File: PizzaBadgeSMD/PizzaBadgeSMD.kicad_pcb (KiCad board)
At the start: 2 copper layers, 52 x 52 mm, 168 parts, among them Q1 NPN, Q2 NPN, Q3 NPN, Q4 NPN, Q5 NPN, Q6 NPN, Q7 NPN, Q8 NPN, SW1 RESET, U1 ESP-12E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

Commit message: fill board
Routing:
- added copper zone on B.Cu, net GND
- added copper zone on F.Cu, net GND

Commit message: update SMD version
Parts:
- added R82: 10K, Resistor_SMD:R_0805_2012Metric, B.Cu at (151.2, 93.6)
- added R83: 10K, Resistor_SMD:R_0805_2012Metric, B.Cu at (125.2, 95.4)
- moved R20 0.60 mm to (155.2, 87.2)
- moved R30 0.54 mm to (155.3, 101.0)
- moved R70 0.50 mm to (122.0, 87.4)
- moved R80 0.41 mm to (131.5, 77.9)
- renumbered GND to J1, 5V to J2
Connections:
- R1 pad 2: Net-(Q1-Pad1) -> Net-(Q1-Pad2)
- R10 pad 1: Net-(Q1-Pad2) -> Net-(Q1-Pad1)
- R11 pad 2: Net-(Q2-Pad1) -> Net-(Q2-Pad2)
- R12 pad 2: Net-(Q2-Pad1) -> Net-(Q2-Pad2)
- R13 pad 2: Net-(Q2-Pad1) -> Net-(Q2-Pad2)
- R14 pad 2: Net-(Q2-Pad1) -> Net-(Q2-Pad2)
- R15 pad 2: Net-(Q2-Pad1) -> Net-(Q2-Pad2)
- R16 pad 2: Net-(Q2-Pad1) -> Net-(Q2-Pad2)
- R17 pad 2: Net-(Q2-Pad1) -> Net-(Q2-Pad2)
- R18 pad 2: Net-(Q2-Pad1) -> Net-(Q2-Pad2)
- R19 pad 2: Net-(Q2-Pad1) -> Net-(Q2-Pad2)
- R2 pad 2: Net-(Q1-Pad1) -> Net-(Q1-Pad2)
- R20 pad 1: Net-(Q2-Pad2) -> Net-(Q2-Pad1)
- R21 pad 2: Net-(Q3-Pad1) -> Net-(Q3-Pad2)
- R22 pad 2: Net-(Q3-Pad1) -> Net-(Q3-Pad2)
- R23 pad 2: Net-(Q3-Pad1) -> Net-(Q3-Pad2)
- R24 pad 2: Net-(Q3-Pad1) -> Net-(Q3-Pad2)
- R25 pad 2: Net-(Q3-Pad1) -> Net-(Q3-Pad2)
- R26 pad 2: Net-(Q3-Pad1) -> Net-(Q3-Pad2)
- R27 pad 2: Net-(Q3-Pad1) -> Net-(Q3-Pad2)
- R28 pad 2: Net-(Q3-Pad1) -> Net-(Q3-Pad2)
- R29 pad 2: Net-(Q3-Pad1) -> Net-(Q3-Pad2)
- R3 pad 2: Net-(Q1-Pad1) -> Net-(Q1-Pad2)
- R30 pad 1: Net-(Q3-Pad2) -> Net-(Q3-Pad1)
- R31 pad 2: Net-(Q4-Pad1) -> Net-(Q4-Pad2)
- R32 pad 2: Net-(Q4-Pad1) -> Net-(Q4-Pad2)
- R33 pad 2: Net-(Q4-Pad1) -> Net-(Q4-Pad2)
- R34 pad 2: Net-(Q4-Pad1) -> Net-(Q4-Pad2)
- R35 pad 2: Net-(Q4-Pad1) -> Net-(Q4-Pad2)
- R36 pad 2: Net-(Q4-Pad1) -> Net-(Q4-Pad2)
- R37 pad 2: Net-(Q4-Pad1) -> Net-(Q4-Pad2)
- R38 pad 2: Net-(Q4-Pad1) -> Net-(Q4-Pad2)
- R39 pad 1: Net-(Q4-Pad2) -> Net-(Q4-Pad1)
- R4 pad 2: Net-(Q1-Pad1) -> Net-(Q1-Pad2)
- R40 pad 2: Net-(Q4-Pad1) -> Net-(Q4-Pad2)
- R41 pad 2: Net-(Q5-Pad1) -> Net-(Q5-Pad2)
- R42 pad 2: Net-(Q5-Pad1) -> Net-(Q5-Pad2)
- R43 pad 2: Net-(Q5-Pad1) -> Net-(Q5-Pad2)
- R44 pad 2: Net-(Q5-Pad1) -> Net-(Q5-Pad2)
- R45 pad 2: Net-(Q5-Pad1) -> Net-(Q5-Pad2)
- R46 pad 2: Net-(Q5-Pad1) -> Net-(Q5-Pad2)
- R47 pad 2: Net-(Q5-Pad1) -> Net-(Q5-Pad2)
- R48 pad 2: Net-(Q5-Pad1) -> Net-(Q5-Pad2)
- R49 pad 2: Net-(Q5-Pad1) -> Net-(Q5-Pad2)
- R5 pad 2: Net-(Q1-Pad1) -> Net-(Q1-Pad2)
- R50 pad 1: Net-(Q5-Pad2) -> Net-(Q5-Pad1)
- R51 pad 2: Net-(Q6-Pad1) -> Net-(Q6-Pad2)
- R52 pad 2: Net-(Q6-Pad1) -> Net-(Q6-Pad2)
- R53 pad 2: Net-(Q6-Pad1) -> Net-(Q6-Pad2)
- R54 pad 2: Net-(Q6-Pad1) -> Net-(Q6-Pad2)
- R55 pad 2: Net-(Q6-Pad1) -> Net-(Q6-Pad2)
- R56 pad 2: Net-(Q6-Pad1) -> Net-(Q6-Pad2)
- R57 pad 2: Net-(Q6-Pad1) -> Net-(Q6-Pad2)
- R58 pad 2: Net-(Q6-Pad1) -> Net-(Q6-Pad2)
- R59 pad 2: Net-(Q6-Pad1) -> Net-(Q6-Pad2)
- R6 pad 2: Net-(Q1-Pad1) -> Net-(Q1-Pad2)
- R60 pad 1: Net-(Q6-Pad2) -> Net-(Q6-Pad1)
- R61 pad 2: Net-(Q7-Pad1) -> Net-(Q7-Pad2)
- R62 pad 2: Net-(Q7-Pad1) -> Net-(Q7-Pad2)
- R63 pad 2: Net-(Q7-Pad1) -> Net-(Q7-Pad2)
- R64 pad 2: Net-(Q7-Pad1) -> Net-(Q7-Pad2)
- R65 pad 2: Net-(Q7-Pad1) -> Net-(Q7-Pad2)
- R66 pad 2: Net-(Q7-Pad1) -> Net-(Q7-Pad2)
- R67 pad 2: Net-(Q7-Pad1) -> Net-(Q7-Pad2)
- R68 pad 2: Net-(Q7-Pad1) -> Net-(Q7-Pad2)
- R69 pad 2: Net-(Q7-Pad1) -> Net-(Q7-Pad2)
- R7 pad 2: Net-(Q1-Pad1) -> Net-(Q1-Pad2)
- R70 pad 1: Net-(Q7-Pad2) -> Net-(Q7-Pad1)
- R71 pad 2: Net-(Q8-Pad1) -> Net-(Q8-Pad2)
- R72 pad 2: Net-(Q8-Pad1) -> Net-(Q8-Pad2)
- R73 pad 2: Net-(Q8-Pad1) -> Net-(Q8-Pad2)
- R74 pad 2: Net-(Q8-Pad1) -> Net-(Q8-Pad2)
- R75 pad 2: Net-(Q8-Pad1) -> Net-(Q8-Pad2)
- R76 pad 2: Net-(Q8-Pad1) -> Net-(Q8-Pad2)
- R77 pad 2: Net-(Q8-Pad1) -> Net-(Q8-Pad2)
- R78 pad 2: Net-(Q8-Pad1) -> Net-(Q8-Pad2)
- R79 pad 2: Net-(Q8-Pad1) -> Net-(Q8-Pad2)
- R8 pad 2: Net-(Q1-Pad1) -> Net-(Q1-Pad2)
- R80 pad 1: Net-(Q8-Pad2) -> Net-(Q8-Pad1)
- R9 pad 2: Net-(Q1-Pad1) -> Net-(Q1-Pad2)
- U1 pad 3: unconnected-(U1-Pad3) -> Net-(U1-Pad3)
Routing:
- net Net-(Q1-Pad2): track 3.88 -> 47.4 mm
- net Net-(Q6-Pad2): track 5.15 -> 47.4 mm
- net Net-(Q5-Pad2): track 4.79 -> 45.9 mm
- net Net-(Q4-Pad2): track 4.68 -> 45.2 mm
- net Net-(Q3-Pad2): track 4.41 -> 43.8 mm
- net Net-(Q7-Pad2): track 4.60 -> 43.2 mm
- net Net-(Q6-Pad1): track 42.6 -> 4.88 mm
- net Net-(Q3-Pad1): track 41.7 -> 4.09 mm
- net Net-(Q1-Pad1): track 41.8 -> 4.15 mm
- net Net-(Q8-Pad2): track 4.19 -> 41.5 mm
- net Net-(Q4-Pad1): track 41.1 -> 4.13 mm
- net Net-(Q2-Pad2): track 4.68 -> 40.2 mm
- net Net-(Q5-Pad1): track 40.5 -> 5.06 mm
- net Net-(Q8-Pad1): track 41.8 -> 8.84 mm
- net Net-(Q7-Pad1): track 40.3 -> 8.84 mm
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
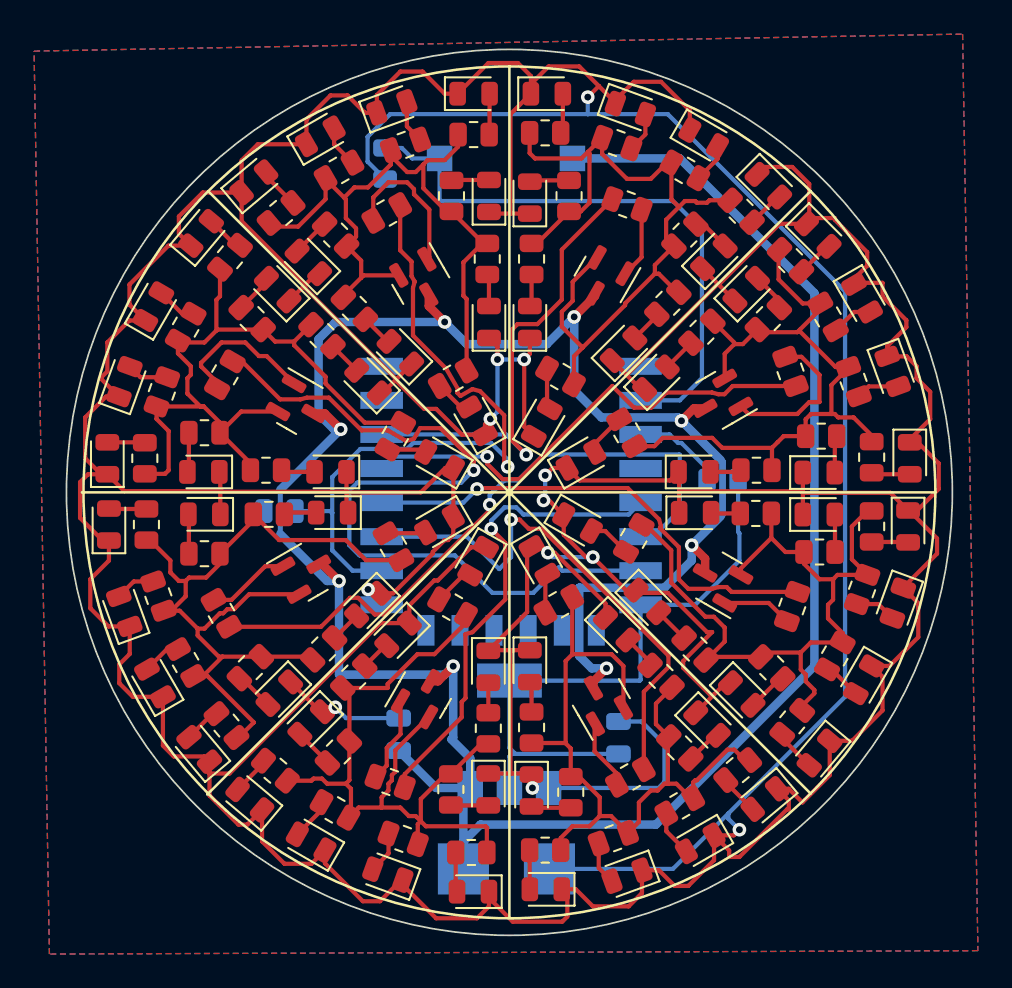
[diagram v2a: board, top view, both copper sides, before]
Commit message: add coin battery
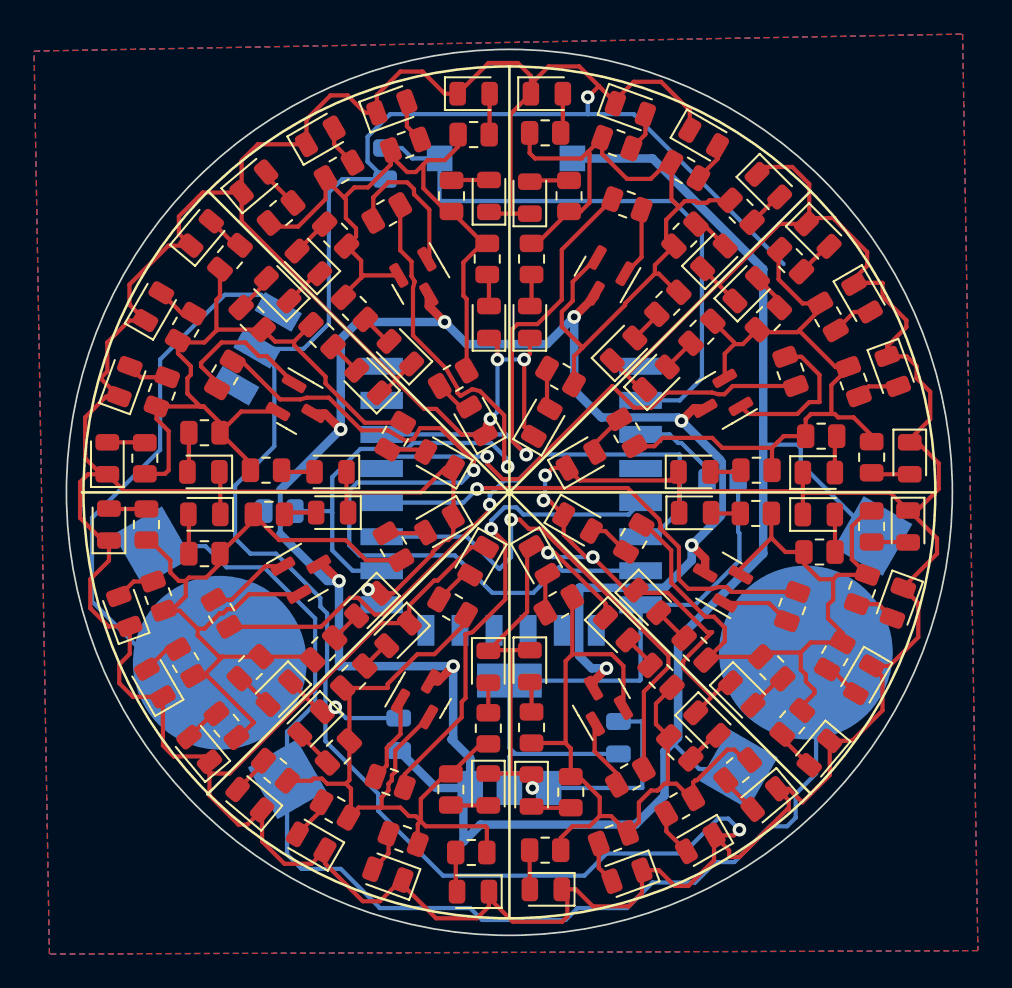
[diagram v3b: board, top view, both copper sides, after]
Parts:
- removed J1: BAT -, TestPoint:TestPoint_Pad_3.0x3.0mm
- removed J2: BAT +, TestPoint:TestPoint_Pad_3.0x3.0mm
- added BT1: Battery_Cell, Battery:BatteryHolder_Keystone_3000_1x12mm, B.Cu at (156.1, 103.7)
- added BT2: Battery_Cell, Battery:BatteryHolder_Keystone_3000_1x12mm, B.Cu at (121.7, 104.3)
- added SW2: Switch, Button_Switch_SMD:SW_SPDT_CK-JS102011SAQN, B.Cu at (121.5, 84.5)
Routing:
- net Net-(BT1-Pad2): track 0.00 -> 70.2 mm
- net Net-(BT2-Pad2): track 0.00 -> 33.8 mm
- net GND: track 523.0 -> 544.0 mm
- net 5V: track 178.0 -> 183.1 mm

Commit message: improve traces
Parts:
- turned R20 to 110 degrees
- turned R70 to -120 degrees
- turned R80 to -150 degrees
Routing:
- net Net-(Q2-Pad1): track 9.14 -> 3.72 mm
- net Net-(Q8-Pad1): track 8.84 -> 3.82 mm
- net Net-(Q7-Pad1): track 8.84 -> 4.14 mm

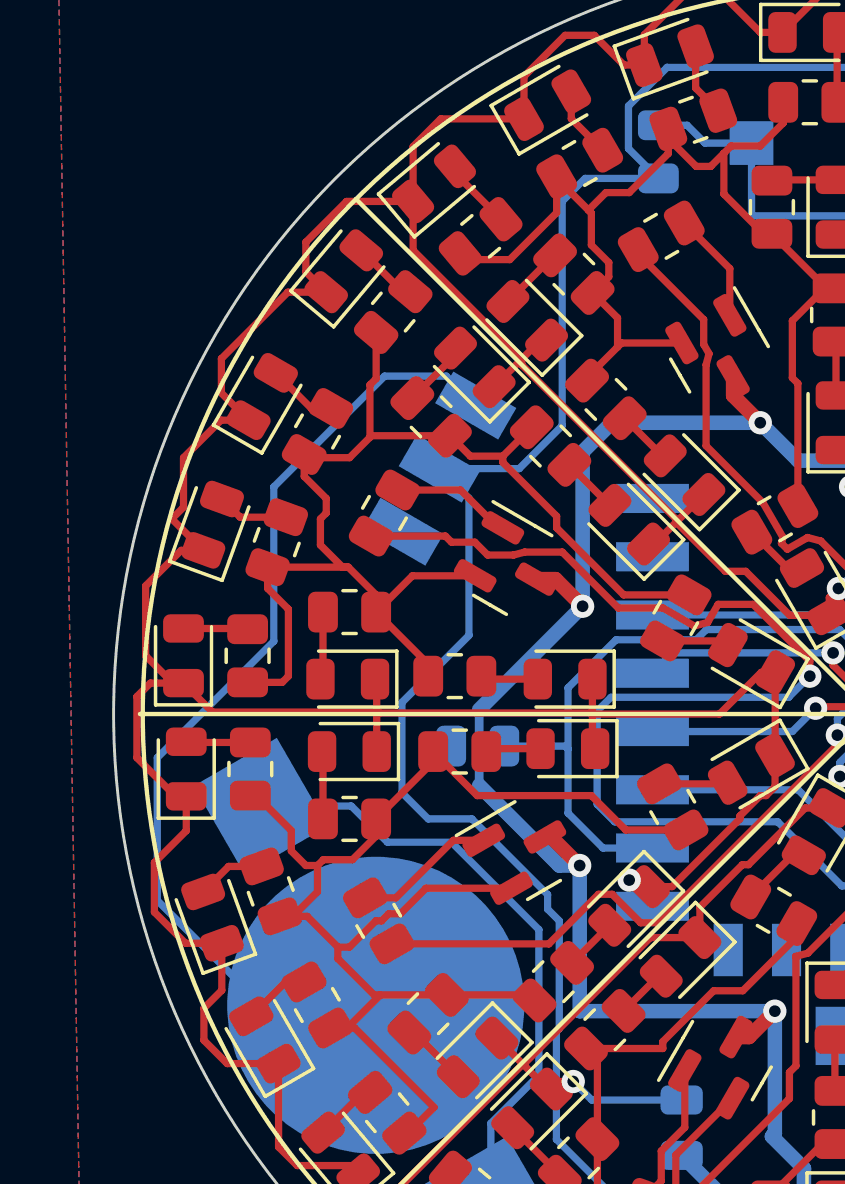
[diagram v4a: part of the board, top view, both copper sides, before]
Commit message: change switch button
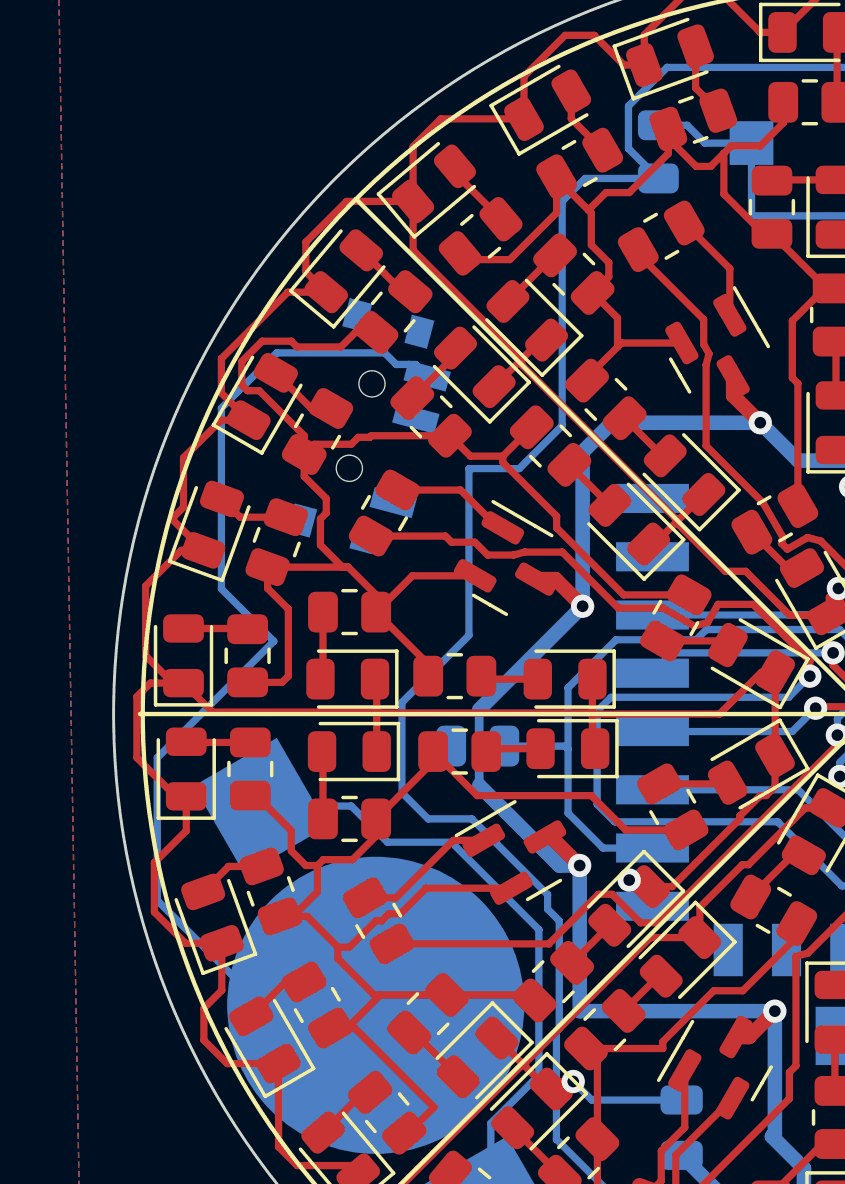
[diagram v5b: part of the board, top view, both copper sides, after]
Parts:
- SW2: footprint Button_Switch_SMD:SW_SPDT_CK-JS102011SAQN -> Button_Switch_SMD:SW_SPDT_PCM12
- turned SW2 to 75 degrees
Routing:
- net Net-(Q7-Pad2): track 43.2 -> 48.9 mm
- net Net-(BT2-Pad2): track 33.8 -> 36.5 mm
- net GND: track 544.0 -> 542.6 mm

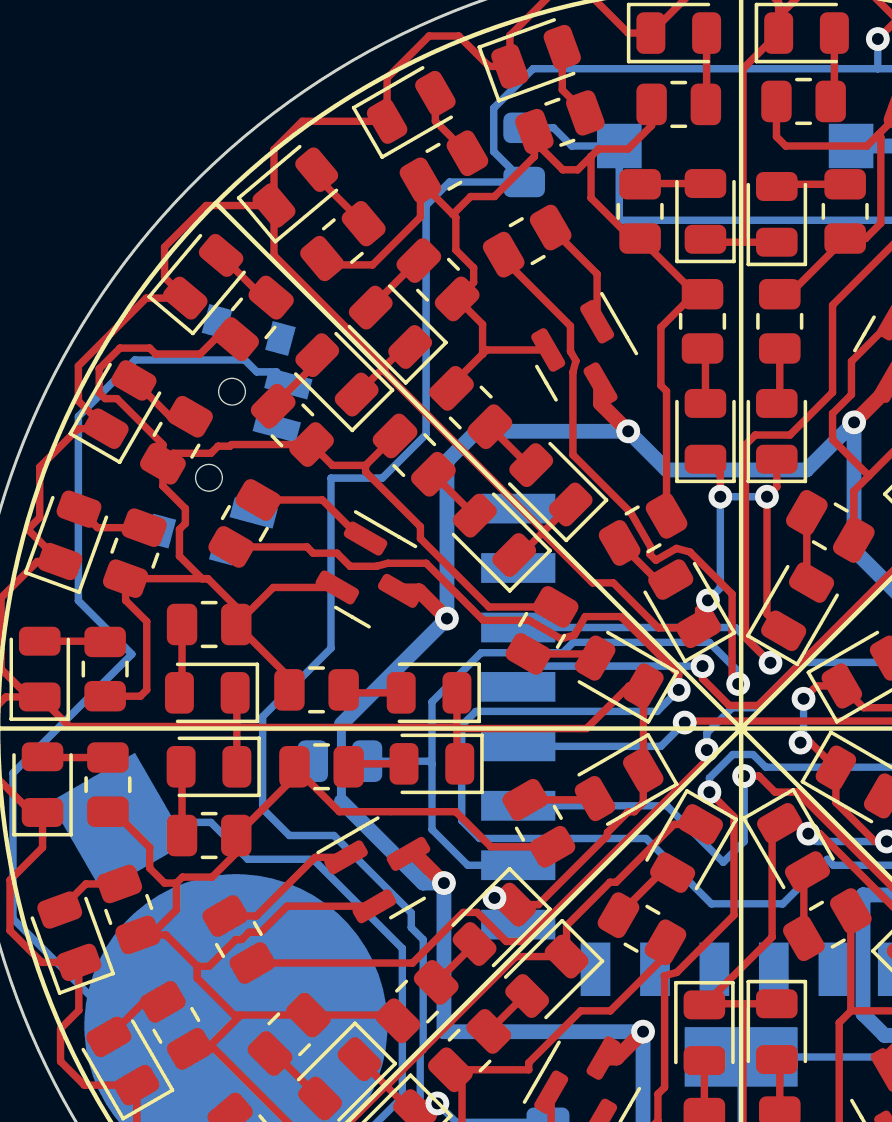
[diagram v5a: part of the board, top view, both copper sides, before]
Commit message: update scheme and board on smd
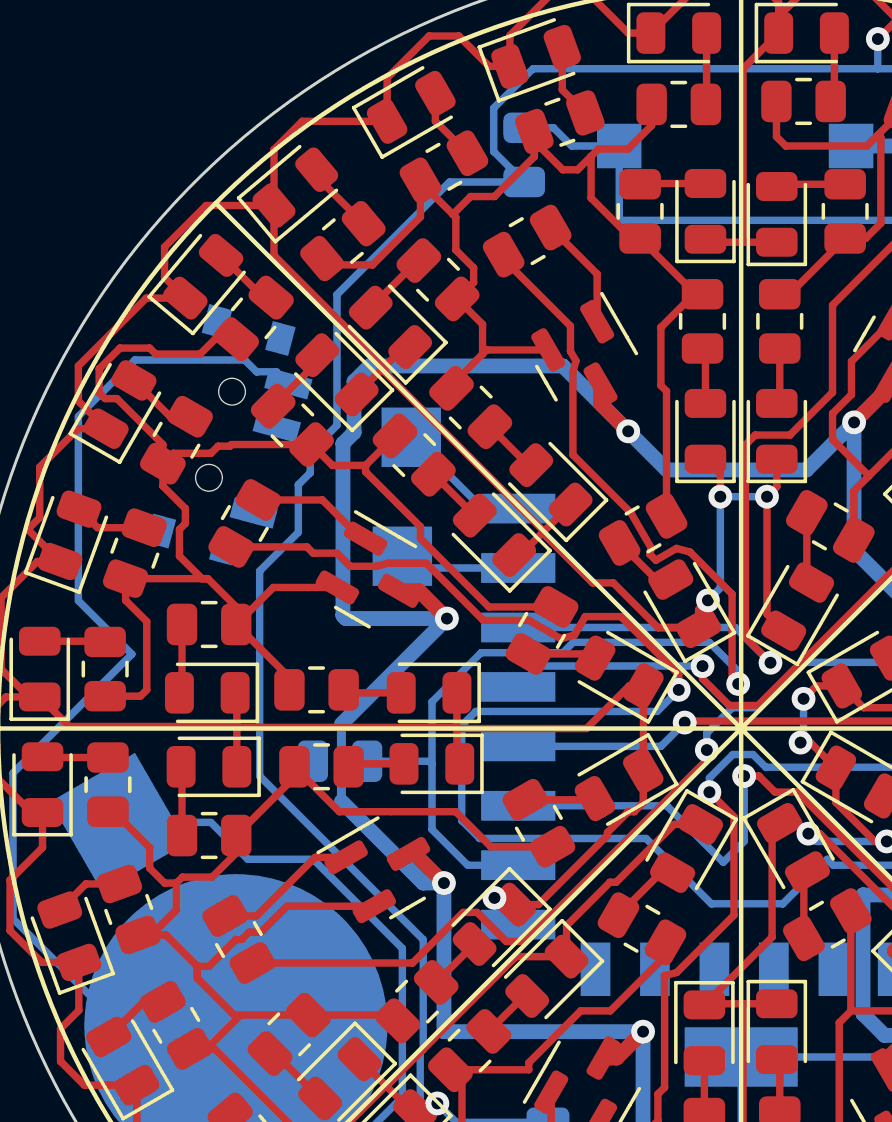
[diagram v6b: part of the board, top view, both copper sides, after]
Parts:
- added J1: TX, TestPoint:TestPoint_Pad_2.0x2.0mm, B.Cu at (127.6, 84.5)
- added J2: RX, TestPoint:TestPoint_Pad_2.0x2.0mm, B.Cu at (127.3, 88.5)
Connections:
- U1 pad 21: unconnected-(U1-Pad21) -> Net-(U1-Pad21)
- U1 pad 22: unconnected-(U1-Pad22) -> Net-(U1-Pad22)
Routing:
- net 5V: track 183.1 -> 193.2 mm
- net Net-(U1-Pad22): track 0.00 -> 4.59 mm
- net Net-(U1-Pad21): track 0.00 -> 4.07 mm
- net GND: track 542.6 -> 540.8 mm
